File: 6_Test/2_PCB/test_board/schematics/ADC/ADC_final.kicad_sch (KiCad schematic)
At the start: 19 parts, among them J1 BNC1, J2 BNC2, J3 TSW-107-07-F-D, J4 TSW-107-07-F-D

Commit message: Corrections to schematic 11_20_24
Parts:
- removed C13, C14, C15, C16, C17, C18: 100pF, symbol Device:C
- removed J1: BNC1, CONN_1274571-1_TYCO, symbol bnc_mini:1274571-1
- removed J2: BNC2, CONN_1274571-1_TYCO, symbol bnc_mini:1274571-1
- removed J3, J4: TSW-107-07-F-D, TSW-107-07-G-D_SAI, symbol 6x2Header:TSW-107-07-F-D
- removed J?: 6130XX21121_61302021121, 6130XX21121_61302021121:61302021121, symbol 2x10Header:6130XX21121_61302021121
- removed R29, R30, R31, R32, R33, R34: 1k, symbol Device:R_US
- added C8: 4.7uF, Capacitor_SMD:C_0201_0603Metric, symbol Device:C
- added C9: 100nF, Capacitor_SMD:C_0201_0603Metric, symbol Device:C
- added J6: GND_AVSS_Connectors, Connector_PinHeader_2.54mm:PinHeader_2x07_P2.54mm_Vertical, symbol Connector_Generic:Conn_02x07_Odd_Even
- renumbered ADC2 to ADC_socket
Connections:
- net AVSS: now also C8.2, C9.2, J6.5 (Pin_5), J6.7 (Pin_7)
- net AVSS_H: now also ADC?.10 (AVSS), J6.8 (Pin_8)
- net AVSS_H1: no longer ADC?.10 (AVSS)
- net GND: now also J6.1 (Pin_1), J6.11 (Pin_11), J6.13 (Pin_13), J6.6 (Pin_6), J6.9 (Pin_9)
- net IOVSS_H1: now also J6.10 (Pin_10)
- net IOVSS_H2: now also J6.14 (Pin_14)
- net PAD_H: now also J6.2 (Pin_2)
- net VLDO: now also C8.1, C9.1
- net VSS_H: now also J6.12 (Pin_12)
- net IN5: now reaches ADC?.7 (IN5)
- net IN5: now also ADC_socket.7 (IN5)
- net IN2: now reaches ADC?.2 (IN2)
- net IN2: now also ADC_socket.2 (IN2)
- net IN4: now reaches ADC?.6 (IN4)
- net IN4: now also ADC_socket.6 (IN4)
- net IN6: now reaches ADC?.8 (IN6)
- net IN6: now also ADC_socket.8 (IN6)
- net IN1: now reaches ADC?.1 (IN1)
- net IN1: now also ADC_socket.1 (IN1)
- net IN3: now reaches ADC?.3 (IN3)
- net IN3: now also ADC_socket.3 (IN3)
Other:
- moved on the sheet: ADC?, ADC_socket

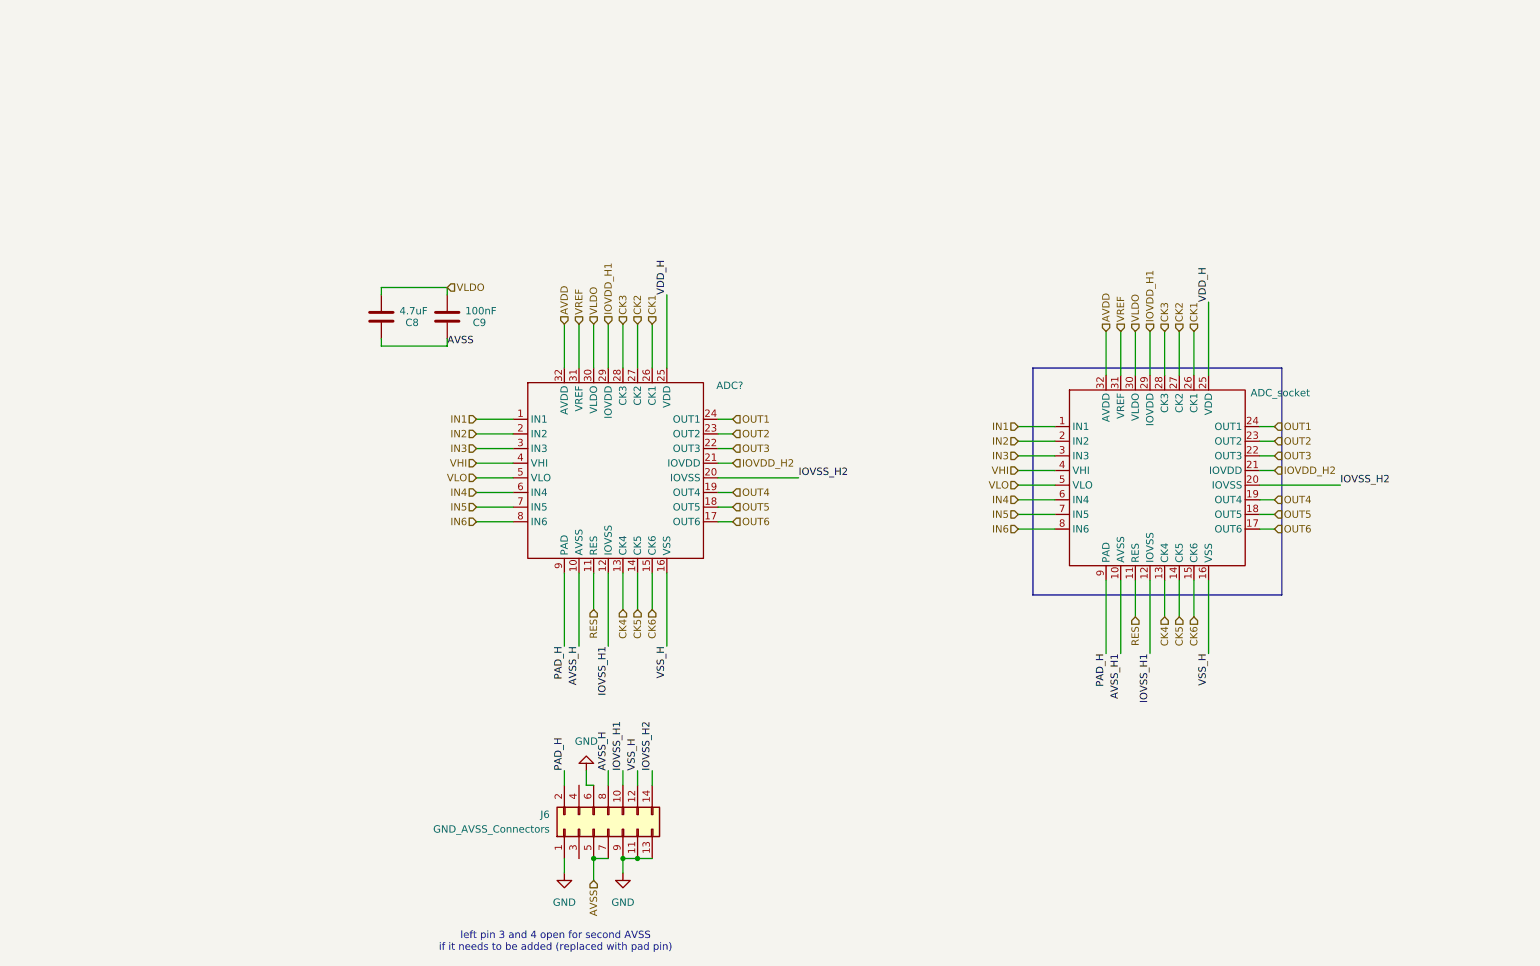
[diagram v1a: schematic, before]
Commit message: Revert "Corrections to schematic 11_20_24"
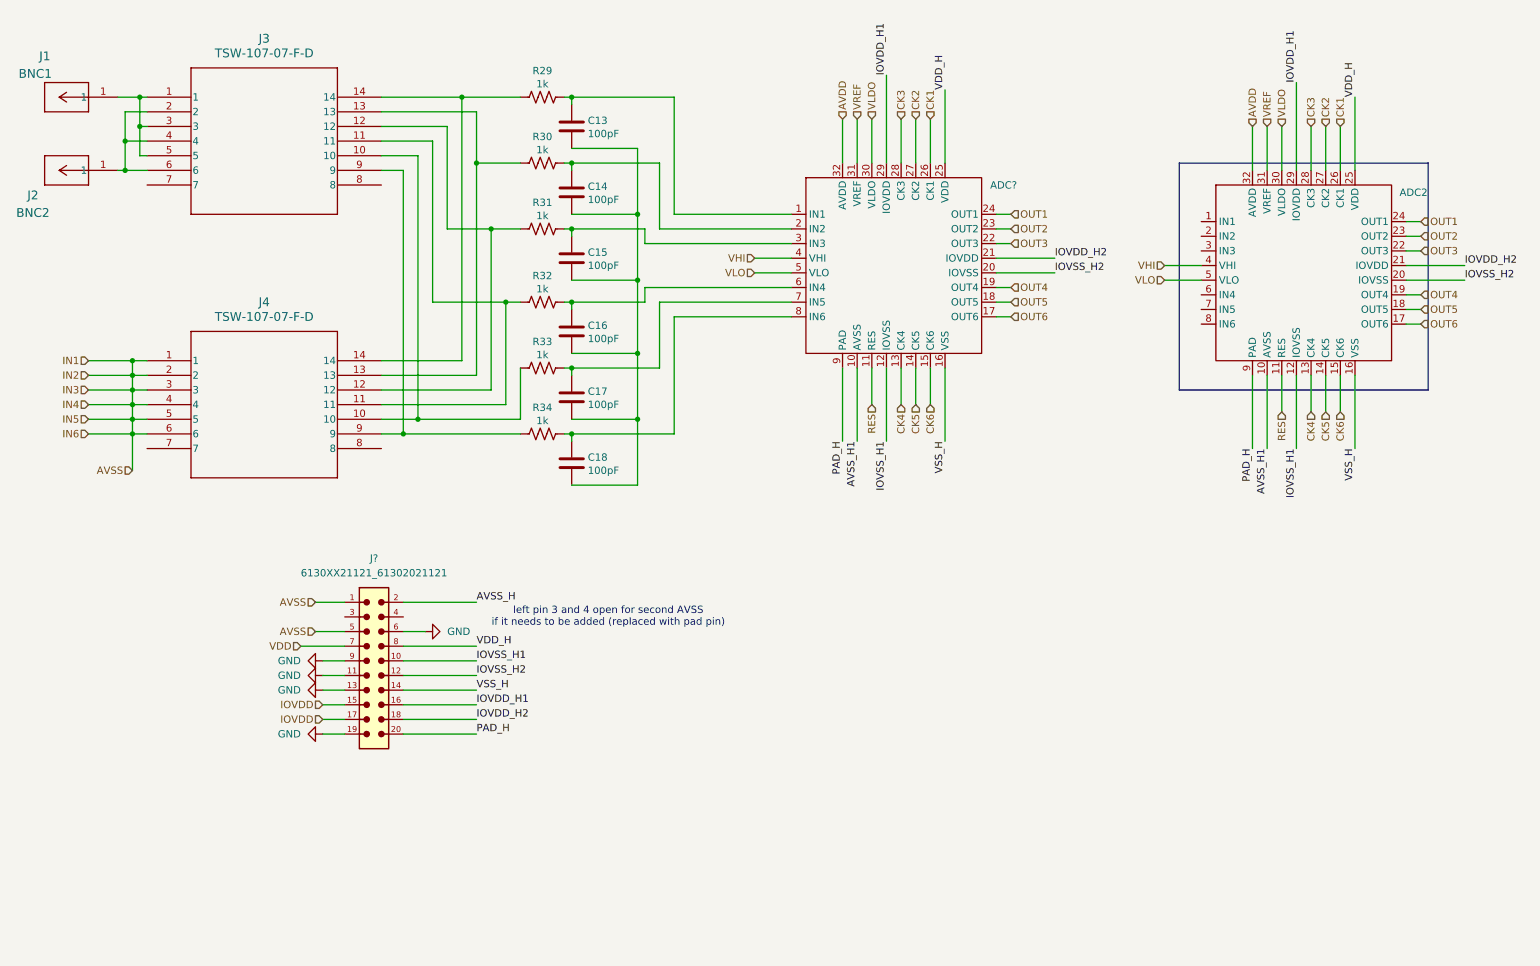
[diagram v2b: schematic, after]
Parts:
- removed C8: 4.7uF, Capacitor_SMD:C_0201_0603Metric, symbol Device:C
- removed C9: 100nF, Capacitor_SMD:C_0201_0603Metric, symbol Device:C
- removed J6: GND_AVSS_Connectors, Connector_PinHeader_2.54mm:PinHeader_2x07_P2.54mm_Vertical, symbol Connector_Generic:Conn_02x07_Odd_Even
- added C13, C14, C15, C16, C17, C18: 100pF, symbol Device:C
- added J1: BNC1, CONN_1274571-1_TYCO, symbol bnc_mini:1274571-1
- added J2: BNC2, CONN_1274571-1_TYCO, symbol bnc_mini:1274571-1
- added J3, J4: TSW-107-07-F-D, TSW-107-07-G-D_SAI, symbol 6x2Header:TSW-107-07-F-D
- added J?: 6130XX21121_61302021121, 6130XX21121_61302021121:61302021121, symbol 2x10Header:6130XX21121_61302021121
- added R29, R30, R31, R32, R33, R34: 1k, symbol Device:R_US
- renumbered ADC_socket to ADC2
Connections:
- net AVSS: now also J4.1, J4.2, J4.3, J4.4, J4.5, J4.6, J?.1, J?.5
- net AVSS_H: now also J?.2; no longer ADC?.10 (AVSS)
- net AVSS_H1: now also ADC?.10 (AVSS)
- net GND: now also J?.11, J?.13, J?.19, J?.6, J?.9
- net IOVDD_H1: now also J?.16
- net IOVDD_H2: now also J?.18
- net IOVSS_H1: now also J?.10
- net IOVSS_H2: now also J?.12
- net PAD_H: now also J?.20
- net VDD_H: now also J?.8
- net VSS_H: now also J?.14
- net IN1: no longer names the net of ADC?.1 (IN1)
- net IN1: now also C13.1, R29.2; no longer ADC2.1 (IN1)
- net IN2: no longer names the net of ADC?.2 (IN2)
- net IN2: now also C14.1, R30.2; no longer ADC2.2 (IN2)
- net IN3: no longer names the net of ADC?.3 (IN3)
- net IN3: now also C15.1, R31.2; no longer ADC2.3 (IN3)
- net IN4: no longer names the net of ADC?.6 (IN4)
- net IN4: now also C16.1, R32.2; no longer ADC2.6 (IN4)
- net IN5: no longer names the net of ADC?.7 (IN5)
- net IN5: now also C17.1, R33.2; no longer ADC2.7 (IN5)
- net IN6: no longer names the net of ADC?.8 (IN6)
- net IN6: now also C18.1, R34.2; no longer ADC2.8 (IN6)
- new net: J3.10, J4.10, R33.1
- new net: J3.13, J4.13, R30.1
- new net: J3.11, J4.11, R32.1
- new net: C13.2, C14.2, C15.2, C16.2, C17.2, C18.2
- new net: J1.1, J3.1, J3.3, J3.5
- new net: J3.12, J4.12, R31.1
- new net: J3.14, J4.14, R29.1
- new net: J2.1, J3.2, J3.4, J3.6
- new net: J3.9, J4.9, R34.1
- new net IOVDD: J?.15, J?.17
- new net VDD: J?.7
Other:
- moved on the sheet: ADC2, ADC?
